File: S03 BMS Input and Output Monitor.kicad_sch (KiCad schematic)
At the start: 29 parts, among them Q4 DMP3018SFV, Q5 DMP3018SFV, U1 LTC1960

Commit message: Use KiCad standard footprints for chip resistors and capacitors
The imported Lattech R/C footprints have poor land patterns (the 0402s
use 0.635 mm circular pads) and cause tombstoning in assembly. Replace
all 139 chip resistors and capacitors with KiCad's standard IPC-7351
nominal footprints:

  Res 0402/0603/1206/2512 -> Resistor_SMD:R_xxxx_xxxxMetric (87)
  Cap 0402/0603/0805/1206/1210 -> Capacitor_SMD:C_xxxx_xxxxMetric (52)

Each part keeps its position, rotation, side, pad nets, schematic link
and reference/value text placement. The pads are on the same axis with
pad 1 on the same side, and every old pad centre lies inside the new
pad, so existing tracks still connect. Zones are refilled.

Schematic Footprint fields and the symbols' footprint filters point at
the new footprints, and the unused imported R/C footprints are removed
from the project library. Electrolytic capacitors are not changed.

DRC: 0 unconnected items, as before. Tracks, vias, zone outlines and
all other footprints are unchanged. 11 courtyard overlaps are new,
because the old footprints had no courtyards.

Co-Authored-By: Claude Opus 5.5 <noreply@anthropic.com>
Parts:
- C10, C4, C5, C55, C57, C6, C7, C8, C9: footprint EVO2513-0_5_0-import-fps:Cap 0402 H0-6 R -> Capacitor_SMD:C_0402_1005Metric
- C11, C12, C3: footprint EVO2513-0_5_0-import-fps:Cap 1206 H1-8 -> Capacitor_SMD:C_1206_3216Metric
- R10, R11, R12, R13, R15, R17, R18, R8, R9: footprint EVO2513-0_5_0-import-fps:Res 0402 H0-45 R -> Resistor_SMD:R_0402_1005Metric
- R14, R16, R23, R82: footprint EVO2513-0_5_0-import-fps:Res 2512 H0-9 -> Resistor_SMD:R_2512_6332Metric
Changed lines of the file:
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@@
 			)
 		)
-		(property "Footprint" "EVO2513-0_5_0-import-fps:Cap 0402 H0-6 R"
+		(property "Footprint" "Capacitor_SMD:C_0402_1005Metric"
 			(at 137.16 96.3422 0)
 			(hide yes)
@@
 			)
 		)
-		(property "Footprint" "EVO2513-0_5_0-import-fps:Res 0402 H0-45 R"
+		(property "Footprint" "Resistor_SMD:R_0402_1005Metric"
 			(at 129.54 197.9422 0)
 			(hide yes)
@@
 			)
 		)
-		(property "Footprint" "EVO2513-0_5_0-import-fps:Cap 0402 H0-6 R"
+		(property "Footprint" "Capacitor_SMD:C_0402_1005Metric"
 			(at 222.25 142.0622 0)
 			(hide yes)
@@
 			)
 		)
-		(property "Footprint" "EVO2513-0_5_0-import-fps:Res 0402 H0-45 R"
+		(property "Footprint" "Resistor_SMD:R_0402_1005Metric"
 			(at 222.25 133.1722 0)
 			(hide yes)
@@
 			)
 		)
-		(property "Footprint" "EVO2513-0_5_0-import-fps:Cap 1206 H1-8"
+		(property "Footprint" "Capacitor_SMD:C_1206_3216Metric"
 			(at 86.36 107.7722 0)
 			(hide yes)
@@
 			)
 		)
-		(property "Footprint" "EVO2513-0_5_0-import-fps:Res 2512 H0-9"
+		(property "Footprint" "Resistor_SMD:R_2512_6332Metric"
 			(at 115.57 78.5622 0)
 			(hide yes)
@@
 			)
 		)
-		(property "Footprint" "EVO2513-0_5_0-import-fps:Res 0402 H0-45 R"
+		(property "Footprint" "Resistor_SMD:R_0402_1005Metric"
 			(at 113.03 197.9422 0)
 			(hide yes)
@@
 			)
 		)
-		(property "Footprint" "EVO2513-0_5_0-import-fps:Cap 0402 H0-6 R"
+		(property "Footprint" "Capacitor_SMD:C_0402_1005Metric"
 			(at 115.57 112.8522 0)
 			(hide yes)
@@
 			)
 		)
-		(property "Footprint" "EVO2513-0_5_0-import-fps:Cap 0402 H0-6 R"
+		(property "Footprint" "Capacitor_SMD:C_0402_1005Metric"
 			(at 166.37 142.0622 0)
 			(hide yes)
@@
 			)
 		)
-		(property "Footprint" "EVO2513-0_5_0-import-fps:Cap 0402 H0-6 R"
+		(property "Footprint" "Capacitor_SMD:C_0402_1005Metric"
 			(at 236.22 134.4422 0)
 			(hide yes)
@@
 			)
 		)
-		(property "Footprint" "EVO2513-0_5_0-import-fps:Cap 1206 H1-8"
+		(property "Footprint" "Capacitor_SMD:C_1206_3216Metric"
 			(at 257.81 185.2422 0)
 			(hide yes)
@@
 			)
 		)
-		(property "Footprint" "EVO2513-0_5_0-import-fps:Res 0402 H0-45 R"
+		(property "Footprint" "Resistor_SMD:R_0402_1005Metric"
 			(at 130.81 128.0922 0)
 			(hide yes)
@@
 			)
 		)
-		(property "Footprint" "EVO2513-0_5_0-import-fps:Cap 0402 H0-6 R"
+		(property "Footprint" "Capacitor_SMD:C_0402_1005Metric"
 			(at 255.27 224.6122 0)
 			(hide yes)
@@
 			)
 		)
-		(property "Footprint" "EVO2513-0_5_0-import-fps:Cap 0402 H0-6 R"
+		(property "Footprint" "Capacitor_SMD:C_0402_1005Metric"
 			(at 120.65 128.0922 0)
 			(hide yes)
@@
 			)
 		)
-		(property "Footprint" "EVO2513-0_5_0-import-fps:Res 0402 H0-45 R"
+		(property "Footprint" "Resistor_SMD:R_0402_1005Metric"
 			(at 154.94 131.9022 0)
 			(hide yes)
@@
 			)
 		)
-		(property "Footprint" "EVO2513-0_5_0-import-fps:Res 2512 H0-9"
+		(property "Footprint" "Resistor_SMD:R_2512_6332Metric"
 			(at 212.09 167.4622 0)
 			(hide yes)
@@
 			)
 		)
-		(property "Footprint" "EVO2513-0_5_0-import-fps:Res 0402 H0-45 R"
+		(property "Footprint" "Resistor_SMD:R_0402_1005Metric"
 			(at 241.3 224.6122 0)
 			(hide yes)
@@
 			)
 		)
-		(property "Footprint" "EVO2513-0_5_0-import-fps:Cap 0402 H0-6 R"
+		(property "Footprint" "Capacitor_SMD:C_0402_1005Metric"
 			(at 143.51 143.3322 0)
 			(hide yes)
@@
 			)
 		)
-		(property "Footprint" "EVO2513-0_5_0-import-fps:Res 0402 H0-45 R"
+		(property "Footprint" "Resistor_SMD:R_0402_1005Metric"
 			(at 130.81 143.3322 0)
 			(hide yes)
@@
 			)
 		)
-		(property "Footprint" "EVO2513-0_5_0-import-fps:Res 2512 H0-9"
+		(property "Footprint" "Resistor_SMD:R_2512_6332Metric"
 			(at 115.57 83.6422 0)
 			(hide yes)
@@
 			)
 		)
-		(property "Footprint" "EVO2513-0_5_0-import-fps:Cap 0402 H0-6 R"
+		(property "Footprint" "Capacitor_SMD:C_0402_1005Metric"
 			(at 154.94 142.0622 0)
 			(hide yes)
@@
 			)
 		)
-		(property "Footprint" "EVO2513-0_5_0-import-fps:Cap 1206 H1-8"
+		(property "Footprint" "Capacitor_SMD:C_1206_3216Metric"
 			(at 270.51 185.2422 0)
 			(hide yes)
@@
 			)
 		)
-		(property "Footprint" "EVO2513-0_5_0-import-fps:Res 0402 H0-45 R"
+		(property "Footprint" "Resistor_SMD:R_0402_1005Metric"
 			(at 104.14 102.6922 0)
 			(hide yes)
@@
 			)
 		)
-		(property "Footprint" "EVO2513-0_5_0-import-fps:Res 0402 H0-45 R"
+		(property "Footprint" "Resistor_SMD:R_0402_1005Metric"
 			(at 241.3 205.5622 0)
 			(hide yes)
@@
 			)
 		)
-		(property "Footprint" "EVO2513-0_5_0-import-fps:Res 2512 H0-9"
+		(property "Footprint" "Resistor_SMD:R_2512_6332Metric"
 			(at 212.09 172.5422 0)
 			(hide yes)

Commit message: Fix schematic ERC issues from the import
ERC across all seven sheets reported 1481 issues from the import:

- Every item sat 43 mil off KiCad's 50 mil connection grid in Y, so new
  wires would not snap to existing pins. Each sheet's contents are
  shifted 7 mil (0.1778 mm) onto the grid; the library symbol
  definitions are untouched and a uniform shift keeps every connection.
  A few wire corners on S06 were off grid on their own (at 6740 mil,
  7620 mil and y 3290 mil); they move to the nearest grid point, which
  removes two 10 mil stubs and moves #PWR065 with its wire.
- Nine wires ran 1.27-2.54 mm past the label sitting on them (ID on S01;
  LDVR1/2 and HDVR1/2 on S06), leaving dangling ends. They are trimmed
  back to the label.
- GND, +12V, +3V3MCU and +5V enter through connector pins, so ERC had
  no power source for them. A PWR_FLAG (#FLG01-#FLG04) sits on each.
- The title-block module name used the Altium formula
  ${COPY(DOCUMENTNAME,5,LENGTH(DOCUMENTNAME)-11)}, which KiCad cannot
  evaluate. Each sheet now carries the title it produced.

ERC: 1481 -> 0. The netlist still matches the PCB's 147 nets.

Update PCB from Schematic was rerun afterwards. It changes metadata only:
footprint filters, unit and pin-function data from the symbols, and the
KiLib_Generator fields dropped from the 139 standard R/C footprints. No
placement or copper changes.

Co-Authored-By: Claude Opus 5.5 <noreply@anthropic.com>
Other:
- note added: "BMS Input and Output Monitor"
- note removed: "${COPY(DOCUMENTNAME,5,LENGTH(DOCUMENTNAME)-11)}"

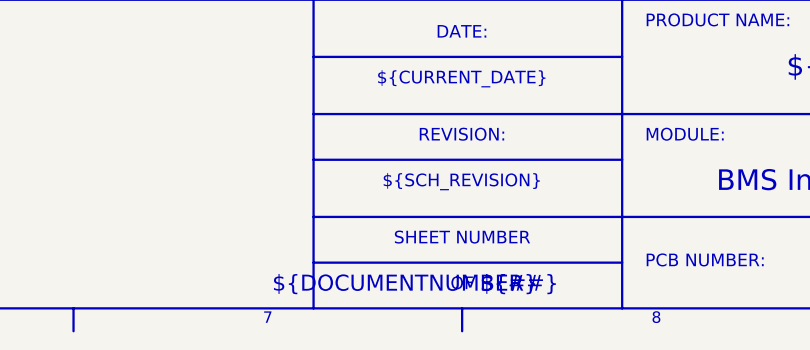
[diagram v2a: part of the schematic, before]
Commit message: Convert the schematic to a hierarchical root sheet
The Altium import produced seven KiCad 10 top-level sheets, with S01's
content in EVO2513-0_5_0.kicad_sch. kicad-cli only loads the first of
those, so command-line ERC, netlist and DRC parity checks saw S01 alone.

- EVO2513-0_5_0.kicad_sch is now a root sheet holding one sheet symbol per
  sheet; S01's content moves to "S01 External Connectors.kicad_sch".
- Each sheet symbol keeps its old top-level sheet UUID, so symbol
  references, net names and connectivity are unchanged: the netlist from
  the new root is identical to the previous whole-design netlist (229
  components, 147 nets). Cross-sheet nets still use global labels.
- The board's 229 footprint paths take the hierarchical form
  /<sheet>/<symbol>, and S01's footprints point at the new sheet file.
  No copper or placement changes.
- Every title block read "sheet 7 of 7" (a single DOCUMENTNUMBER project
  variable). Sheet numbers now use the page number: the root is page 1
  and S01-S07 are pages 2-8.

kicad-cli ERC over the whole design: 0 errors, 0 warnings. DRC with
schematic parity: 0 parity issues, 450 violations as before.

Co-Authored-By: Claude Opus 5.5 <noreply@anthropic.com>
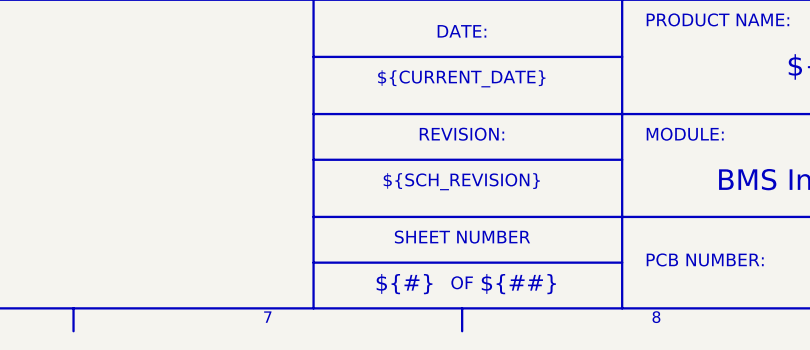
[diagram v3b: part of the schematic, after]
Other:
- note added: "${#}"
- note removed: "${DOCUMENTNUMBER}"

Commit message: Link the sheets through hierarchical labels and sheet pins
The 78 cross-sheet global labels on S01-S07 become hierarchical labels,
and each sheet symbol on the root gets a pin per label name (71 pins).
On the root, each pin connects through a short wire to a global label
with the net name. Global labels there, rather than local ones, keep the
35 net names free of a "/" sheet-path prefix, so the net classes and the
board's nets are unchanged.

Layout: S01 External Connectors on the left with its pins on the right
edge; S02-S04 and S05-S07 in two columns with their pins on the left.

The netlist is identical to before (229 components, 147 nets, same names
and pins). kicad-cli ERC: 0 errors, 0 warnings. DRC with schematic
parity: 0 parity issues, 450 violations as before.

Co-Authored-By: Claude Opus 5.5 <noreply@anthropic.com>
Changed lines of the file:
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@@
 		)
 	)
-	(global_label "DCSENSED"
+	(hierarchical_label "DCSENSED"
 		(shape passive)
 		(at 342.9 71.12 0)
-		(fields_autoplaced yes)
 		(effects
 			(font
@@
 			(justify left)
 		)
-		(property "Intersheetrefs" "${INTERSHEET_REFS}"
-			(at 342.9 71.12 0)
-			(effects
-				(font
-					(size 1.27 1.27)
-				)
-				(justify left)
-				(hide yes)
-			)
-		)
 	)
-	(global_label "CLOCK"
+	(hierarchical_label "CLOCK"
 		(shape passive)
 		(at 81.28 217.17 180)
-		(fields_autoplaced yes)
 		(effects
 			(font
@@
 			(justify right)
 		)
-		(property "Intersheetrefs" "${INTERSHEET_REFS}"
-			(at 81.28 217.17 0)
-			(effects
-				(font
-					(size 1.27 1.27)
-				)
-				(justify right)
-				(hide yes)
-			)
-		)
 	)
-	(global_label "nCS"
+	(hierarchical_label "nCS"
 		(shape passive)
 		(at 81.28 220.98 180)
-		(fields_autoplaced yes)
 		(effects
 			(font
@@
 			(justify right)
 		)
-		(property "Intersheetrefs" "${INTERSHEET_REFS}"
-			(at 81.28 220.98 0)
-			(effects
-				(font
-					(size 1.27 1.27)
-				)
-				(justify right)
-				(hide yes)
-			)
-		)
 	)
-	(global_label "MISO"
+	(hierarchical_label "MISO"
 		(shape passive)
 		(at 81.28 210.82 180)
-		(fields_autoplaced yes)
 		(effects
 			(font
@@
 			(justify right)
 		)
-		(property "Intersheetrefs" "${INTERSHEET_REFS}"
-			(at 81.28 210.82 0)
-			(effects
-				(font
-					(size 1.27 1.27)
-				)
-				(justify right)
-				(hide yes)
-			)
-		)
 	)
-	(global_label "DCFILTERED"
+	(hierarchical_label "DCFILTERED"
 		(shape passive)
 		(at 55.88 83.82 180)
-		(fields_autoplaced yes)
 		(effects
 			(font
@@
 			(justify right)
 		)
-		(property "Intersheetrefs" "${INTERSHEET_REFS}"
-			(at 55.88 83.82 0)
-			(effects
-				(font
-					(size 1.27 1.27)
-				)
-				(justify right)
-				(hide yes)
-			)
-		)
 	)
-	(global_label "DCBMS"
+	(hierarchical_label "DCBMS"
 		(shape passive)
 		(at 304.8 172.72 0)
-		(fields_autoplaced yes)
 		(effects
 			(font
@@
 			(justify left)
 		)
-		(property "Intersheetrefs" "${INTERSHEET_REFS}"
-			(at 304.8 172.72 0)
-			(effects
-				(font
-					(size 1.27 1.27)
-				)
-				(justify left)
-				(hide yes)
-			)
-		)
 	)
-	(global_label "DCPATH"
+	(hierarchical_label "DCPATH"
 		(shape passive)
 		(at 81.28 172.72 180)
-		(fields_autoplaced yes)
 		(effects
 			(font
@@
 			(justify right)
 		)
-		(property "Intersheetrefs" "${INTERSHEET_REFS}"
-			(at 81.28 172.72 0)
-			(effects
-				(font
-					(size 1.27 1.27)
-				)
-				(justify right)
-				(hide yes)
-			)
-		)
 	)
-	(global_label "DCPATH"
+	(hierarchical_label "DCPATH"
 		(shape passive)
 		(at 342.9 83.82 0)
-		(fields_autoplaced yes)
 		(effects
 			(font
@@
 			(justify left)
 		)
-		(property "Intersheetrefs" "${INTERSHEET_REFS}"
-			(at 342.9 83.82 0)
-			(effects
-				(font
-					(size 1.27 1.27)
-				)
-				(justify left)
-				(hide yes)
-			)
-		)
 	)
-	(global_label "MOSI"
+	(hierarchical_label "MOSI"
 		(shape passive)
 		(at 81.28 207.01 180)
-		(fields_autoplaced yes)
 		(effects
 			(font
@@
 			(justify right)
 		)
-		(property "Intersheetrefs" "${INTERSHEET_REFS}"
-			(at 81.28 207.01 0)
-			(effects
-				(font
-					(size 1.27 1.27)
-				)
-				(justify right)
-				(hide yes)
-			)
-		)
 	)
